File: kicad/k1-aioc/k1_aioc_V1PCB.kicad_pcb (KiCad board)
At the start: 2 copper layers, 50.8 x 71.1 mm, 56 parts, among them J1 Conn_01x07_Male, J2 12401832E402A, J3 SIP 200, J4 SIP 200, Q1 BC847BS, U1 MIC5330-SSYML, U2 STM32F373CBTx(OLD), Y1 8MHz/20pF

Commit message: adding files for backup
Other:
- board size 50.8 x 71.1 mm -> 54.6 x 72.4 mm
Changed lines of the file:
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@@
     )
   )
-  (gr_rect (start 164.46 129.28) (end 113.66 58.16) (layer "Edge.Cuts") (width 0.1) (fill none))
+  (gr_rect (start 167 130.55) (end 112.39 58.16) (layer "Edge.Cuts") (width 0.1) (fill none))
 )

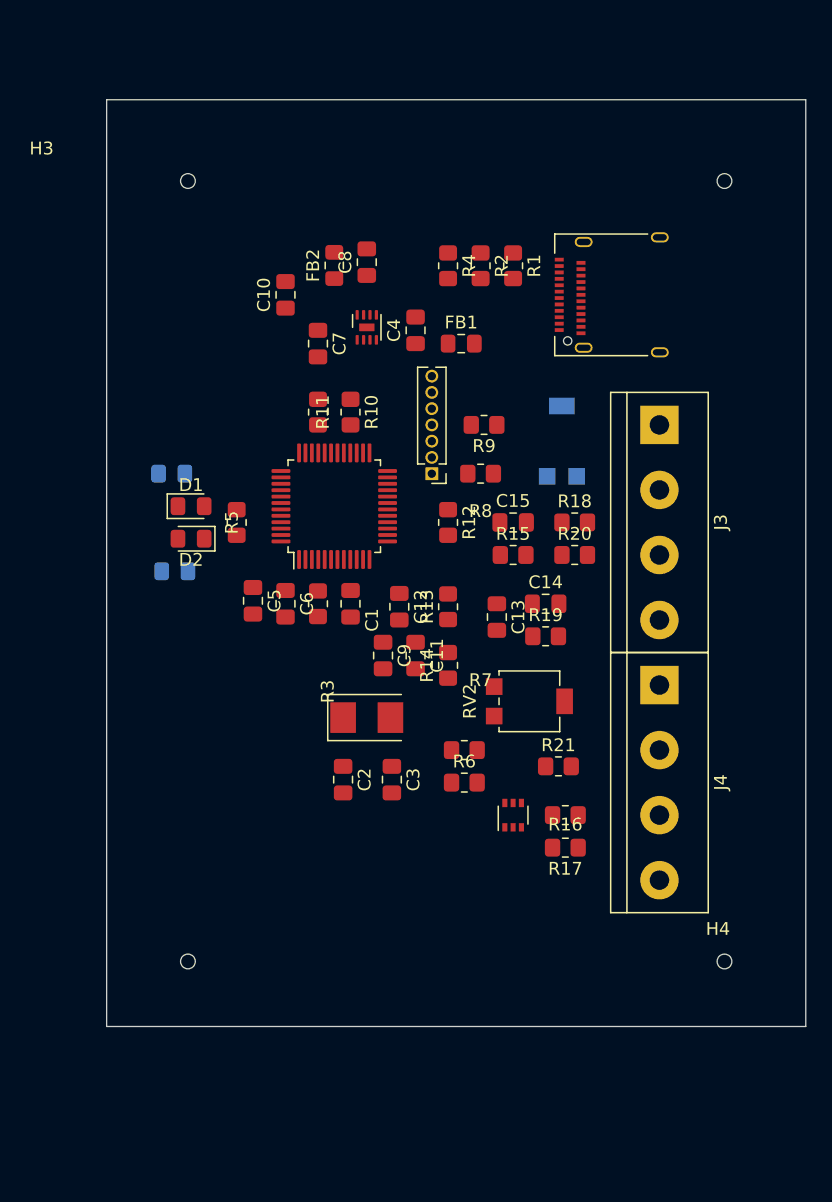
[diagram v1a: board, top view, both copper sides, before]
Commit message: updating files and adding usb datasheet
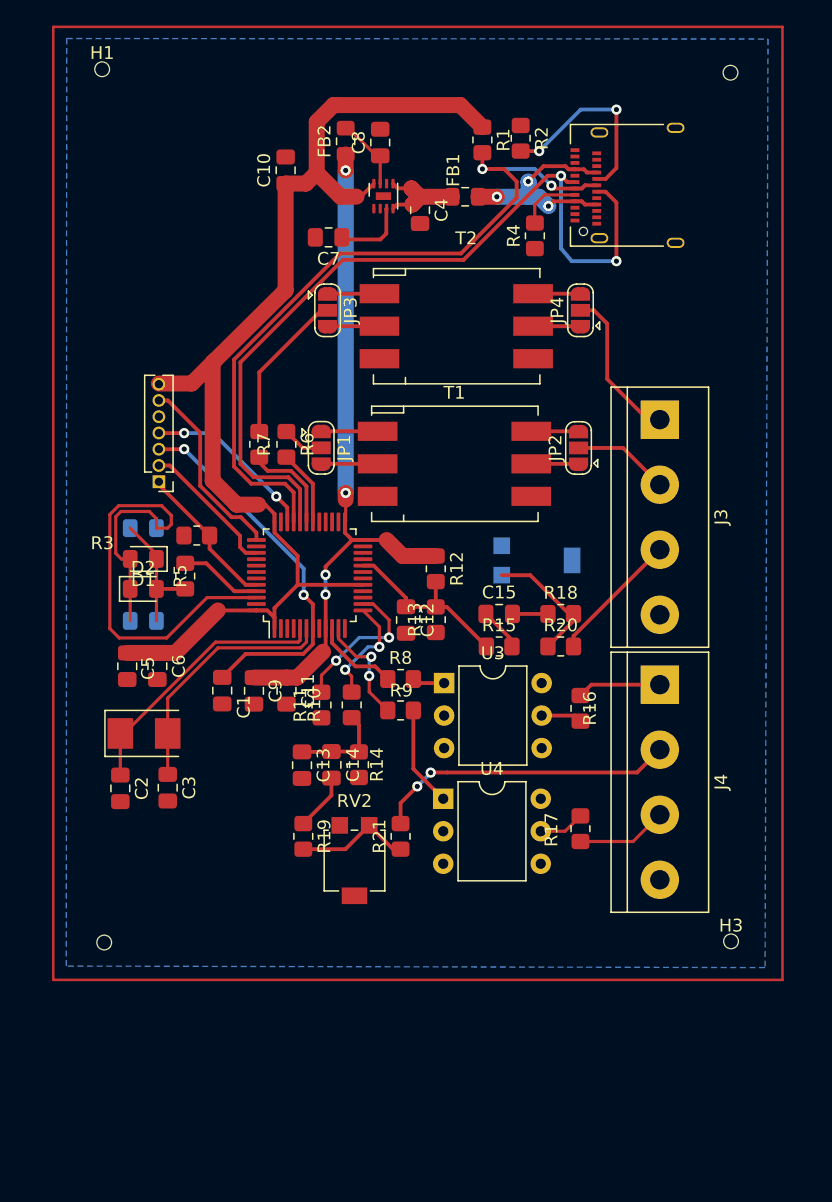
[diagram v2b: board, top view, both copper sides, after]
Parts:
- removed Q1: BC847BS, Package_TO_SOT_SMD:SOT-363_SC-70-6
- added JP1: SolderJumper_3_Open, Jumper:SolderJumper-3_P1.3mm_Open_RoundedPad1.0x1.5mm, F.Cu at (129.2, 85.3)
- added JP2: SolderJumper_3_Open, Jumper:SolderJumper-3_P1.3mm_Open_RoundedPad1.0x1.5mm, F.Cu at (149.2, 85.4)
- added JP3: SolderJumper_3_Open, Jumper:SolderJumper-3_P1.3mm_Open_RoundedPad1.0x1.5mm, F.Cu at (129.7, 74.6)
- added JP4: SolderJumper_3_Open, Jumper:SolderJumper-3_P1.3mm_Open_RoundedPad1.0x1.5mm, F.Cu at (149.4, 74.6)
- added T1: Transformer_Audio_CTP_CTS, AIOC:Transformer_Bourns_SM-LP-5001, F.Cu at (139.6, 86.6)
- added T2: Transformer_Audio_CTP_CTS, AIOC:Transformer_Bourns_SM-LP-5001, F.Cu at (139.7, 75.8)
- added U3: 4N25, Package_DIP:DIP-6_W7.62mm, F.Cu at (138.8, 103.7)
- added U4: 4N25, Package_DIP:DIP-6_W7.62mm, F.Cu at (138.7, 112.8)
- moved R11 25.3 mm to (129.2, 105.4), turned to 90 degrees
- moved R19 24.5 mm to (127.8, 115.7), turned to -90 degrees
- moved J1 21.3 mm to (116.5, 88.0)
- moved C14 20.9 mm to (129.9, 110.1), turned to -90 degrees
- moved R10 20.7 mm to (131.5, 105.4), turned to 90 degrees
- moved C13 19.1 mm to (127.7, 110.1)
- moved RV2 18.5 mm to (131.8, 117.6), turned to 0 degrees
- moved C3 17.5 mm to (117.2, 111.9)
- moved Y1 17.4 mm to (115.3, 107.7)
- moved C2 17.4 mm to (113.5, 111.9)
- moved R21 13.5 mm to (135.3, 115.7), turned to 90 degrees
- moved C1 12.1 mm to (121.4, 104.3)
- moved FB1 11.5 mm to (140.4, 65.7)
- moved C6 11.1 mm to (116.3, 102.4)
- moved C5 11.1 mm to (114.0, 102.4)
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- renumbered H3 to H1, H1 to H2, H4 to H3, H2 to H4, R8 to R10, R9 to R11, R10 to R6, R11 to R7, R6 to R8, R7 to R9
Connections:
- J3 pad 1: /RADIO-RX-PTT1 -> Net-(JP4-Pad2)
- J3 pad 2: /RADIO-TX -> /RADIO-RX-PTT1
- J4 pad 4: GND -> GNDS
- R6 pad 1: /RADIO-RX-PTT1 -> Net-(JP1-Pad2)
- R7 pad 1: /RADIO-TX -> Net-(JP3-Pad2)
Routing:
- net +3V3: track 0.00 -> 91.6 mm
- net /USB-DN: track 0.00 -> 65.3 mm, vias 0 -> 2
- net /USB-DP: track 0.00 -> 58.8 mm, vias 0 -> 2
- net +3.3VA: track 0.00 -> 53.4 mm, vias 0 -> 4
- net Net-(D1-Pad2): track 0.00 -> 42.7 mm
- net /NRST: track 0.00 -> 29.5 mm, vias 0 -> 2
- net Net-(J4-Pad2): track 0.00 -> 23.6 mm, vias 0 -> 2
- net /OSCIN: track 0.00 -> 21.2 mm
- net /OSCOUT: track 0.00 -> 19.7 mm
- net /VBUS: track 0.00 -> 17.1 mm, vias 0 -> 3
- net Net-(J2-PadB5): track 0.00 -> 15.3 mm, vias 0 -> 2
- net /SWCLK: track 0.00 -> 14.9 mm
- net /AFIN: track 0.00 -> 14.6 mm
- net /RADIO-RX-PTT1: track 0.00 -> 14.6 mm
- net /SWDIO: track 0.00 -> 13.6 mm, vias 0 -> 2
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- added copper zone on B.Cu, net GND
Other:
- board outline removed

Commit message: Updating Kicad files for review
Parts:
- removed the R16 at (149.4, 105.7)
- removed the R17 at (149.4, 115.1)
- added D5: 1N4001, Diode_SMD:D_0805_2012Metric_Pad1.15x1.40mm_HandSolder, F.Cu at (126.1, 125.7)
- added D6: 1N4001, Diode_SMD:D_0805_2012Metric_Pad1.15x1.40mm_HandSolder, F.Cu at (135.5, 125.6)
- added J5: SIP 200, TerminalBlock:TerminalBlock_bornier-3_P5.08mm, F.Cu at (158.3, 93.8)
- added J6: SIP 200, TerminalBlock:TerminalBlock_bornier-2_P5.08mm, F.Cu at (158.3, 109.4)
- added J7: SIP 200, TerminalBlock:TerminalBlock_bornier-3_P5.08mm, F.Cu at (158.3, 119.9)
- added R18: 1K2, Resistor_SMD:R_0805_2012Metric_Pad1.20x1.40mm_HandSolder, F.Cu at (128.1, 128.1)
- added R19: 1K2, Resistor_SMD:R_0805_2012Metric_Pad1.20x1.40mm_HandSolder, F.Cu at (135.5, 128.1)
- D3, D4: moved to F.Cu
- H1, H2, H3, H4: footprint AIOC:TOOLING-HOLE -> MountingHole:MountingHole_3.2mm_M3_DIN965_Pad_TopBottom
- J3: value SIP 200 -> conn_01X02; footprint TerminalBlock:TerminalBlock_bornier-4_P5.08mm -> Connector_PinHeader_2.54mm:PinHeader_1x02_P2.54mm_Vertical
- J4: footprint TerminalBlock:TerminalBlock_bornier-4_P5.08mm -> TerminalBlock:TerminalBlock_bornier-2_P5.08mm
- RV2: renamed from RV1; moved to F.Cu
- U3, U4: footprint Package_DIP:DIP-6_W7.62mm -> Package_DIP:DIP-6_W8.89mm_SMDSocket_LongPads
- Y1: footprint AIOC:Crystal_SMD_5032-2Pin_5.0x3.2mm -> AIOC:Crystal_8MHz_SMD_11.40mm
- moved J3 42.4 mm to (113.3, 85.1), turned to 180 degrees
- moved JP3 39.1 mm to (144.9, 124.2), turned to 0 degrees
- moved T1 29.0 mm to (146.1, 114.9), turned to -90 degrees
- moved JP1 28.3 mm to (149.4, 105.2), turned to 180 degrees
- moved J4 20.7 mm to (158.3, 83.3)
- moved R16 19.6 mm to (143.9, 126.9), turned to 180 degrees
- moved U3 18.4 mm to (127.1, 117.9), turned to -90 degrees
- moved R20 17.6 mm to (146.5, 129.3), turned to 0 degrees
- moved RV1 17.6 mm to (141.7, 132.0)
- moved C14 16.6 mm to (145.4, 103.9)
- moved C13 16.6 mm to (143.0, 103.9)
- moved C1 16.2 mm to (115.8, 89.1)
- moved R1 15.5 mm to (145.1, 76.4), turned to 90 degrees
- moved R11 13.8 mm to (140.7, 97.8), turned to 180 degrees
- moved H3 13.2 mm to (159.0, 136.9)
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- renumbered JP3 to JP2, JP2 to JP3, R19 to R16, R18 to R17, R21 to R20, R20 to R21, RV2 to RV1
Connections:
- J3 pad 1: Net-(JP4-Pad2) -> /NRST
- J3 pad 2: /RADIO-RX-PTT1 -> GND
- J4 pad 1: /RADIO-VP-PTT2 -> Net-(J4-Pad1)
- JP1 pad 2: Net-(JP1-Pad2) -> Net-(C14-Pad2)
- JP2 pad 2: Net-(JP3-Pad2) -> Net-(C15-Pad2)
- JP3 pad 2: /RADIO-RX-PTT1 -> Net-(JP3-Pad2)
- R16 pad 1: Net-(C14-Pad2) -> Net-(JP3-Pad2)
- R17 pad 1: Net-(C15-Pad2) -> Net-(JP4-Pad2)
- R20 pad 2: Net-(J4-Pad2) -> Net-(J7-Pad1)
- R21 pad 2: Net-(J3-Pad3) -> Net-(J5-Pad1)
- R6 pad 1: Net-(JP1-Pad2) -> Net-(J4-Pad2)
- R7 pad 1: Net-(JP3-Pad2) -> Net-(J4-Pad1)
- RV1 pad 2: GND -> GNDS
- RV1 pad 3: GND -> GNDS
- RV2 pad 2: GND -> GNDS
- RV2 pad 3: GND -> GNDS
- T1 pad 4: GND -> GNDS
- T2 pad 4: GND -> GNDS
- U3 pad 5: Net-(R16-Pad2) -> /RADIO-VP-PTT2
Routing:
- net GND: track 0.00 -> 69.8 mm, vias 0 -> 20
- net Net-(J6-Pad2): track 0.00 -> 43.4 mm
- net Net-(D6-Pad1): track 3.60 -> 42.1 mm
- net /RADIO-VP-PTT2: track 6.55 -> 42.8 mm
- net Net-(J4-Pad1): track 0.00 -> 36.0 mm
- net Net-(D1-Pad2): track 42.7 -> 24.1 mm
- net +3V3: track 91.6 -> 74.1 mm, vias 0 -> 4
- net /USB-DP: track 58.8 -> 43.1 mm, vias 2 -> 0
- net Net-(J7-Pad1): track 0.00 -> 15.6 mm
- net /RADIO-RX-PTT1: track 14.6 -> 0.00 mm
- net Net-(J4-Pad2): track 23.6 -> 37.2 mm, vias 2 -> 0
- net Net-(C15-Pad2): track 2.77 -> 13.5 mm
- net Net-(J3-Pad3): track 10.3 -> 0.00 mm
- net /OSCOUT: track 19.7 -> 9.45 mm
- net Net-(J5-Pad1): track 0.00 -> 10.1 mm
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- added copper zone on F.Cu, net GNDS
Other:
- board outline added: 56 x 85 mm
- board text added: "1"
- board text added: "2"
- board text added: "3"
- board text added: "4"
- board text added: "5"
- board text added: "6"
- board text added: "7"
- board text added: "GND"
- board text added: "GNDS"
- board text added: "Giga Technology"
- board text added: "PRX"
- board text added: "PTT IN"
- board text added: "PTT1"
- board text added: "PTT2"
- board text added: "PTX"
- board text added: "Program"
- board text added: "RRX"
- board text added: "RTX"
- board text added: "Radio Int"
- board text added: "Reset"
- board text added: "SN:__________"
- board text added: "VER: 1.0"

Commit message: Updating PCB files
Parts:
- JP1, JP2, JP3, JP4: value SolderJumper_3_Open -> SolderJumper_3_Bridged12; footprint Jumper:SolderJumper-3_P1.3mm_Open_RoundedPad1.0x1.5mm -> Jumper:SolderJumper-3_P1.3mm_Bridged12_RoundedPad1.0x1.5mm_NumberLabels
- moved R2 1.28 mm to (144.7, 68.2)
- moved R9 0.35 mm to (139.1, 107.9)
- moved JP4 0.21 mm to (151.1, 84.9), turned to -90 degrees
- moved JP1 0.12 mm to (149.4, 105.3)
- moved R15 0.07 mm to (140.7, 95.0)
- turned JP3 to 180 degrees
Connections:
- T1 pad 5: Net-(JP3-Pad1) -> Net-(JP3-Pad3)
- T1 pad 6: Net-(JP3-Pad3) -> Net-(JP3-Pad1)
- T2 pad 5: Net-(JP4-Pad1) -> Net-(JP4-Pad3)
- T2 pad 6: Net-(JP4-Pad3) -> Net-(JP4-Pad1)
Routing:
- net Net-(C15-Pad2): track 13.5 -> 15.2 mm
- net GND: track 69.8 -> 68.4 mm
- net Net-(J2-PadB5): track 15.4 -> 16.3 mm
